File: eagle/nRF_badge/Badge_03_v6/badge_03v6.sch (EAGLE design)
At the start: 43 parts, among them J1 PROG_CONN_6, U1 LIS2DH12", U2 LP2985LV, U3 MCP6231, U5 M95M02, Y1 32768Hz

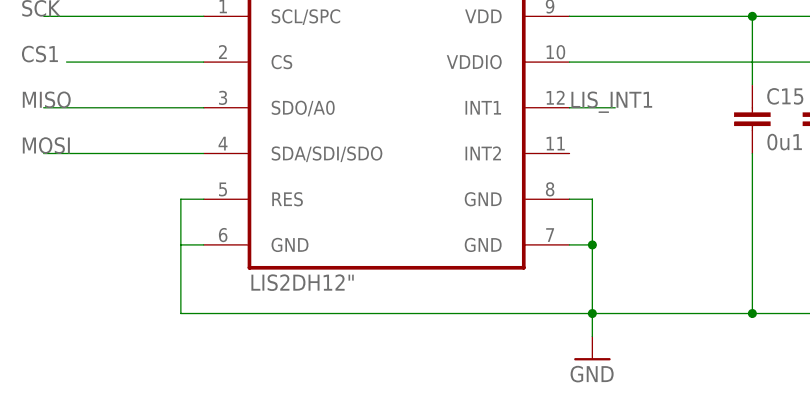
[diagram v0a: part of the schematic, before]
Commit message: Changes LIS2DH12 footprints to fit the devkit's traces
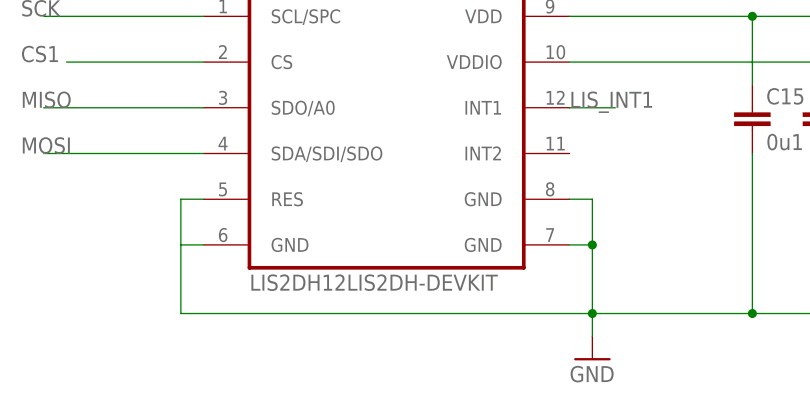
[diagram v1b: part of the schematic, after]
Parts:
- U1: value LIS2DH12" -> LIS2DH12LIS2DH-DEVKIT; device Badge:LIS2DH12" -> Badge:LIS2DH12LIS2DH-DEVKIT
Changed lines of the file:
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@@
 <part name="C17" library="rcl" library_urn="urn:adsk.eagle:library:334" deviceset="C-EU" device="C0603" package3d_urn="urn:adsk.eagle:package:23616/2" value="0u1"/>
 <part name="SUPPLY18" library="Badge" deviceset="VCC" device=""/>
-<part name="U1" library="Badge" deviceset="LIS2DH12" device="&quot;"/>
+<part name="U1" library="Badge" deviceset="LIS2DH12" device="LIS2DH-DEVKIT"/>
 </parts>
 <sheets>
